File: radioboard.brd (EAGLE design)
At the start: 160 x 100 mm, 22 parts, among them Q1 8MHz, U1 STM32F302_303C2

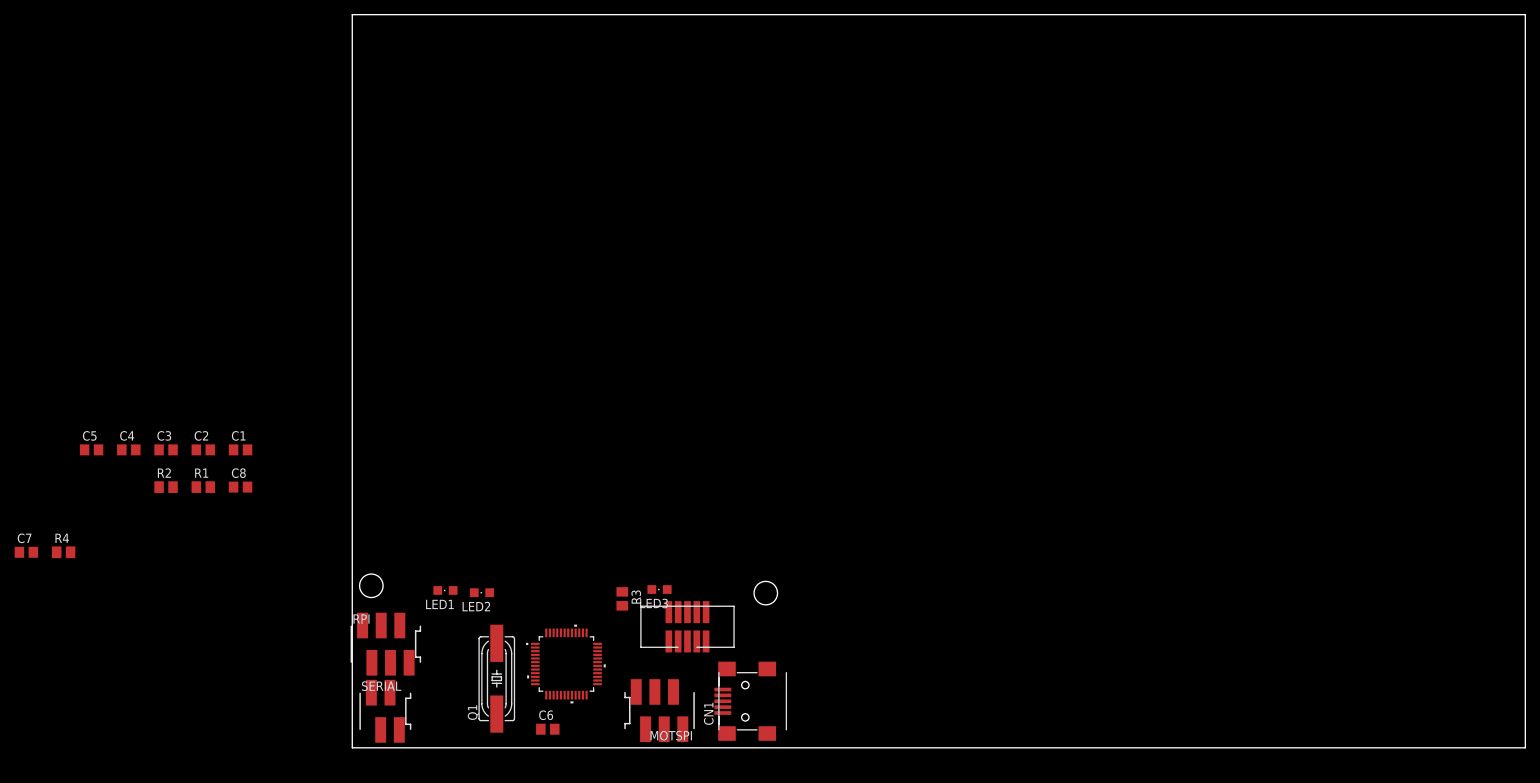
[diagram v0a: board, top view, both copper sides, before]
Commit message: finished schematic, continued placing
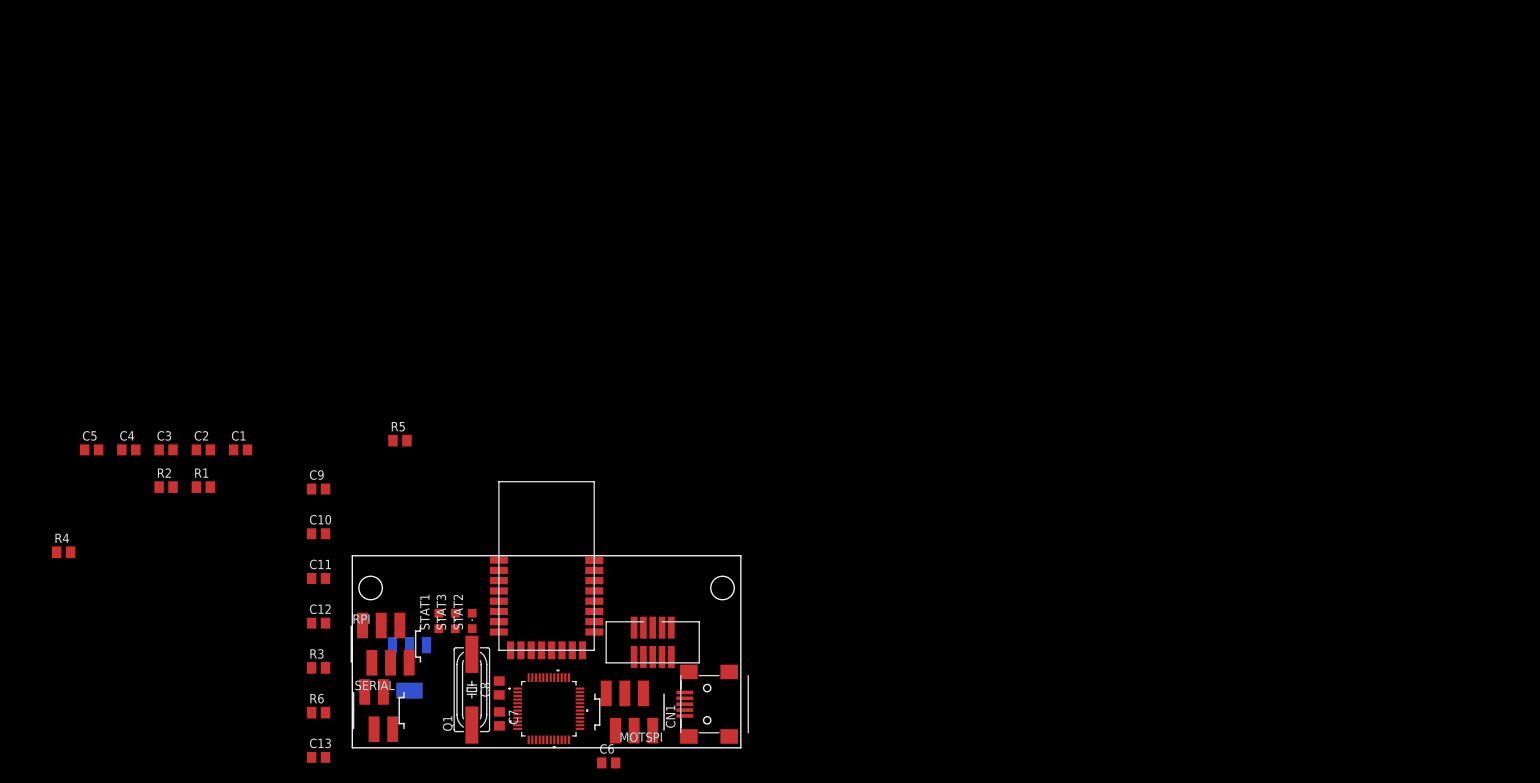
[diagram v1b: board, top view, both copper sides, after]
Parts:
- removed LED1, LED2, LED3: (no value), misc:CHIPLED_0805
- added C10, C12, C9: 10u, rcl:C0805
- added C11, C13: 100n, rcl:C0805
- added DWM1000: DWM1000, DWM1000:DW1000-PACKAGE
- added IC1: VREG-TS1117CW-3V3, we-power:SOT223
- added R5: 1k, rcl:M0805
- added R6: 47k, rcl:M0805
- added STAT1, STAT2, STAT3: (no value), misc:CHIPLED_0805
- R3: value 1k -> 47k
- U1: value STM32F302_303C2 -> STM32F302C8
- moved C7 68.4 mm to (20.1, 3.95), turned to 270 degrees
- moved C8 44.7 mm to (20.0, 8.16), turned to 90 degrees
- moved R3 42.5 mm to (-4.60, 10.9), turned to 0 degrees
- moved C6 9.49 mm to (35.0, -2.06)
- moved U1 6.56 mm to (26.8, 5.33)
- moved CN1 5.22 mm to (49.4, 5.95)
- moved U$1 5.19 mm to (41.0, 14.4), turned to 270 degrees
- moved MOTSPI 4.10 mm to (37.8, 4.88)
- moved Q1 3.72 mm to (16.3, 7.93)
- moved SERIAL 0.91 mm to (3.61, 5.08)
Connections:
- removed net N$15: U1.30
- removed net N$9: LED3.A, R3.1
- new net DWM_IRQ: DWM1000.IRQ, U1.38
- new net DWM_MISO: DWM1000.SPIMISO, U1.40
- new net DWM_MOSI: DWM1000.SPIMOSI, U1.41
- new net DWM_N_CS: DWM1000.SPICSN, U1.42
- new net DWM_N_RST: DWM1000.RSTN, U1.43
- new net DWM_SCK: DWM1000.SPICLK, U1.39
- new net N$10: R5.2, STAT1.A
- new net N$5: R5.1, U1.4
- net +3V3: now also C10.1, C11.1, C12.1, DWM1000.VDD3V3, DWM1000.VDD3V32, DWM1000.VDDAON, IC1.2, IC1.4
- net +5V: now also C9.1, IC1.3, R6.1
- net GND: now also C10.2, C11.2, C12.2, C13.2, C9.2, DWM1000.VSS1, DWM1000.VSS2, DWM1000.VSS3, DWM1000.VSS4, DWM1000.VSS5, IC1.1, R3.2, STAT1.C, STAT2.C, STAT3.C; no longer LED1.C, LED2.C, LED3.C
- net N$6: now also STAT3.A; no longer LED1.A
- net N$7: now also STAT2.A; no longer LED2.A
- net N$8: now also C13.1, R3.1, R6.2, U1.13; no longer R3.2, U1.38
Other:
- board size 160 x 100 mm -> 53 x 26.2 mm

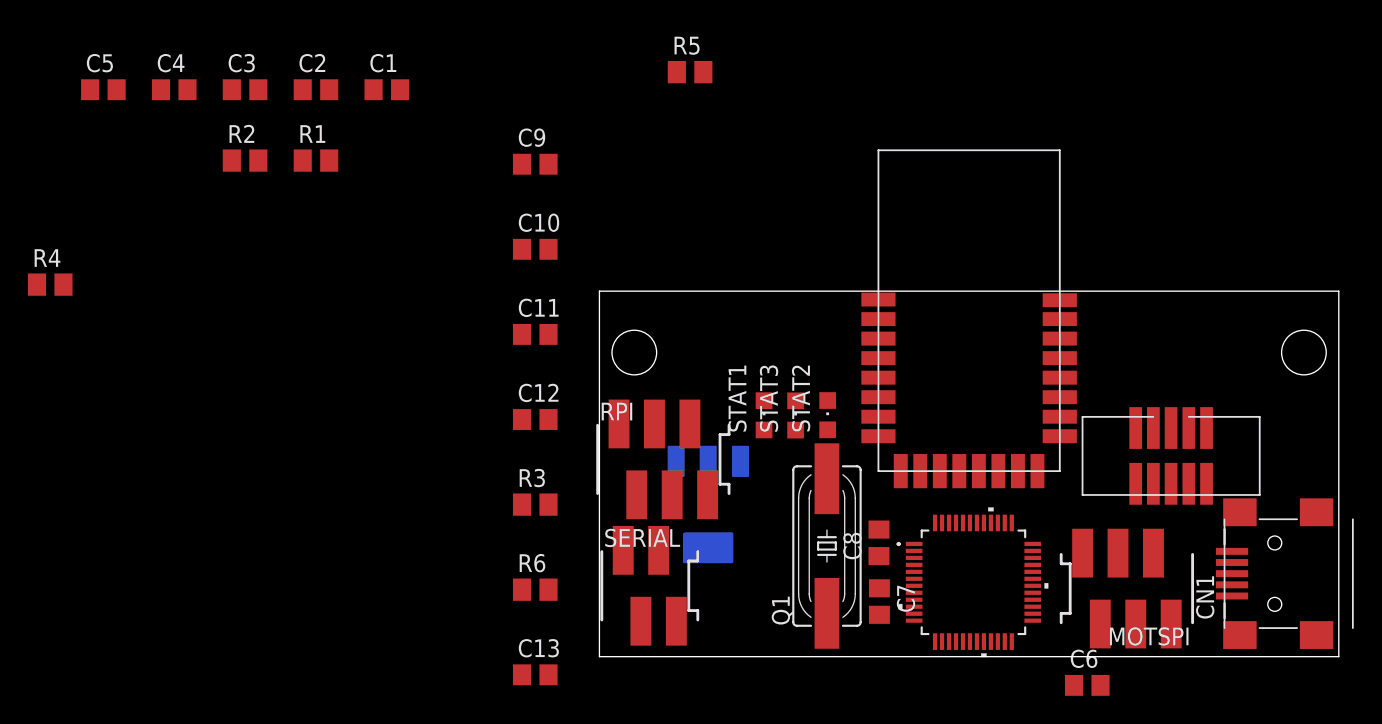
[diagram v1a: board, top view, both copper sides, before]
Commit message: placed and routed PCB, added design rules
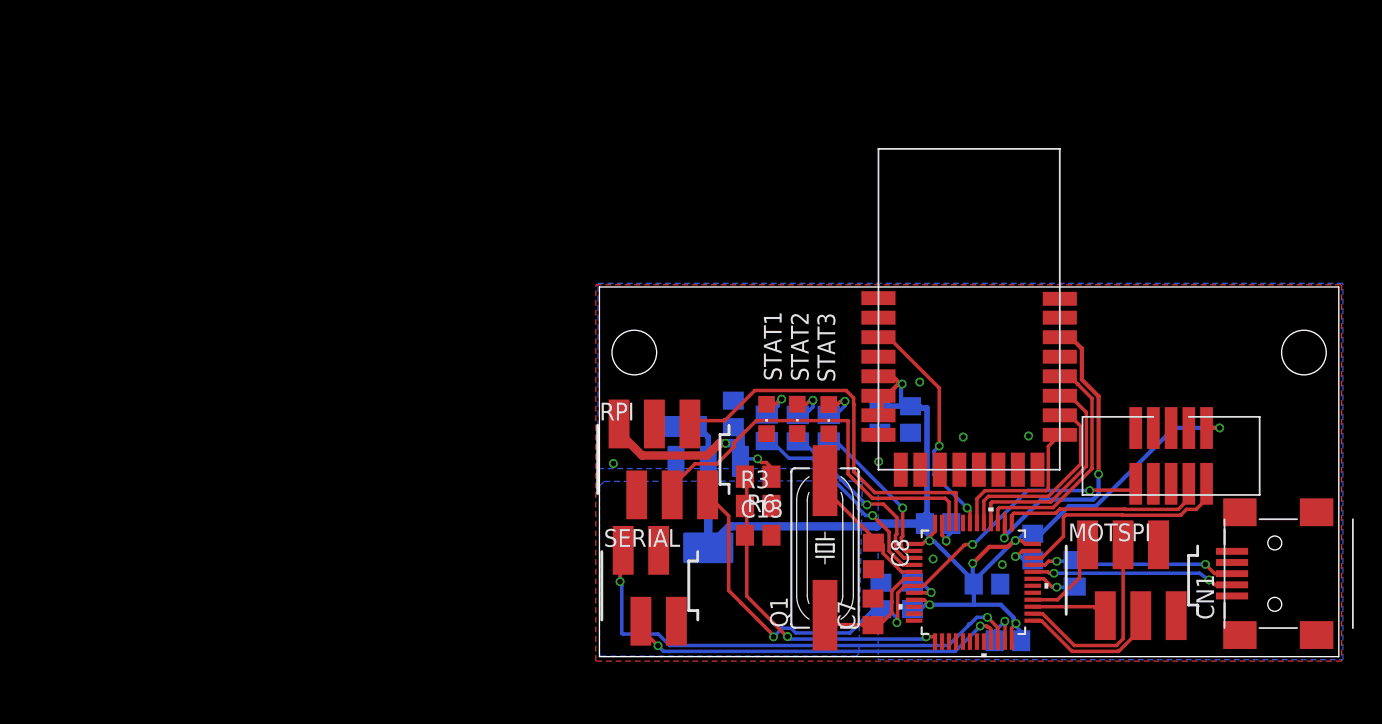
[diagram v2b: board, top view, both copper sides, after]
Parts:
- moved R4 76.3 mm to (34.1, 5.97), flipped to the bottom, turned to 270 degrees
- moved C5 72.6 mm to (27.8, 5.20), flipped to the bottom, turned to 180 degrees
- moved C2 63.4 mm to (29.3, 1.14), flipped to the bottom
- moved C4 63.0 mm to (24.3, 9.54), flipped to the bottom, turned to 180 degrees
- moved C3 60.0 mm to (22.4, 4.36), flipped to the bottom, turned to 90 degrees
- moved C1 56.7 mm to (31.1, 7.86), flipped to the bottom, turned to 270 degrees
- moved R2 44.0 mm to (14.2, 16.4), flipped to the bottom, turned to 90 degrees
- moved R1 41.5 mm to (16.4, 16.4), flipped to the bottom, turned to 90 degrees
- moved C11 27.6 mm to (22.3, 17.0), flipped to the bottom, turned to 270 degrees
- moved R5 26.1 mm to (12.0, 16.4), flipped to the bottom, turned to 90 degrees
- moved C12 24.7 mm to (20.1, 17.0), flipped to the bottom, turned to 270 degrees
- moved C9 22.8 mm to (9.60, 17.4), flipped to the bottom, turned to 90 degrees
- moved C13 18.9 mm to (11.4, 8.70)
- moved R6 17.9 mm to (11.4, 12.9), turned to 180 degrees
- moved C10 16.6 mm to (6.10, 16.5), flipped to the bottom
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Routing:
- net +3V3: track 0.00 -> 97.7 mm, vias 0 -> 7
- net N_RESET: track 0.00 -> 45.5 mm, vias 0 -> 4
- net RPI_TX: track 0.00 -> 35.7 mm, vias 0 -> 2
- net RPI_SDA: track 0.00 -> 29.3 mm
- net RPI_SCL: track 0.00 -> 28.6 mm
- net RPI_RX: track 0.00 -> 28.0 mm, vias 0 -> 2
- net N$8: track 0.00 -> 24.4 mm, vias 0 -> 2
- net DWM_IRQ: track 0.00 -> 22.8 mm, vias 0 -> 2
- net DWM_SCK: track 0.00 -> 16.9 mm
- net DWM_N_RST: track 0.00 -> 16.8 mm, vias 0 -> 2
- net +5V: track 0.00 -> 16.7 mm, vias 0 -> 2
- net SWD_IO: track 0.00 -> 16.1 mm
- net N$5: track 0.00 -> 15.8 mm, vias 0 -> 1
- net DWM_MISO: track 0.00 -> 15.7 mm
- net USB_DP: track 0.00 -> 14.8 mm, vias 0 -> 2
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- added copper zone on layer 16, net +3V3
- added copper zone on layer 1, net GND
- added copper zone on layer 16, net GND
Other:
- board size 53 x 26.2 mm -> 53 x 26.5 mm

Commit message: finished PCB
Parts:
- added ON: (no value), misc:CHIPLED_0805
- added R7: 2.2k, rcl:M0805
- moved C6 1.08 mm to (19.7, 3.39)
- moved C9 0.36 mm to (9.24, 17.4)
- renumbered STAT1 to SYNC, STAT2 to RX/TX, STAT3 to BATT
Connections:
- new net N$9: ON.C, R7.2
- net +3V3: now also ON.A
- net GND: now also R7.1
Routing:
- net GND: track 11.9 -> 25.4 mm, vias 11 -> 71
- net +3V3: track 97.7 -> 102.3 mm
- net N$9: track 0.00 -> 2.82 mm, vias 0 -> 1
- net RPI_SCL: track 28.6 -> 27.0 mm
- net RPI_SDA: track 29.3 -> 28.1 mm
- net RPI_TX: track 35.7 -> 36.8 mm
- net DWM_IRQ: track 22.8 -> 22.1 mm
- net N_RESET: track 45.5 -> 45.0 mm
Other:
- board text added: "2017"
- board text added: "RTLS v1"
- board text added: "TelecomRobotics"
